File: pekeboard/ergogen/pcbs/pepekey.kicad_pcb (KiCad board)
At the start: 2 copper layers, 150.9 x 124.7 mm, 63 parts

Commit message: pekepad folder fix
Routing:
- net (no net): track 0.00 -> 337.7 mm
- net P008: track 268.6 -> 42.3 mm
- net P031: track 206.8 -> 0.00 mm, vias 6 -> 0
- net P100: track 258.8 -> 52.9 mm, vias 6 -> 5
- net P011: track 258.2 -> 52.9 mm, vias 6 -> 5
- net P106: track 251.5 -> 52.9 mm, vias 7 -> 5
- net P022: track 240.4 -> 42.3 mm, vias 5 -> 4
- net P024: track 230.4 -> 42.3 mm
- net P115: track 164.6 -> 0.00 mm, vias 6 -> 0
- net P002: track 158.9 -> 0.00 mm, vias 6 -> 0
- net P113: track 154.5 -> 0.00 mm, vias 3 -> 0
- net P025: track 120.0 -> 0.00 mm, vias 6 -> 0
- net GND: track 89.7 -> 0.00 mm, vias 2 -> 0
- net RAW: track 56.1 -> 0.00 mm, vias 1 -> 0
- net RST: track 47.5 -> 0.00 mm
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
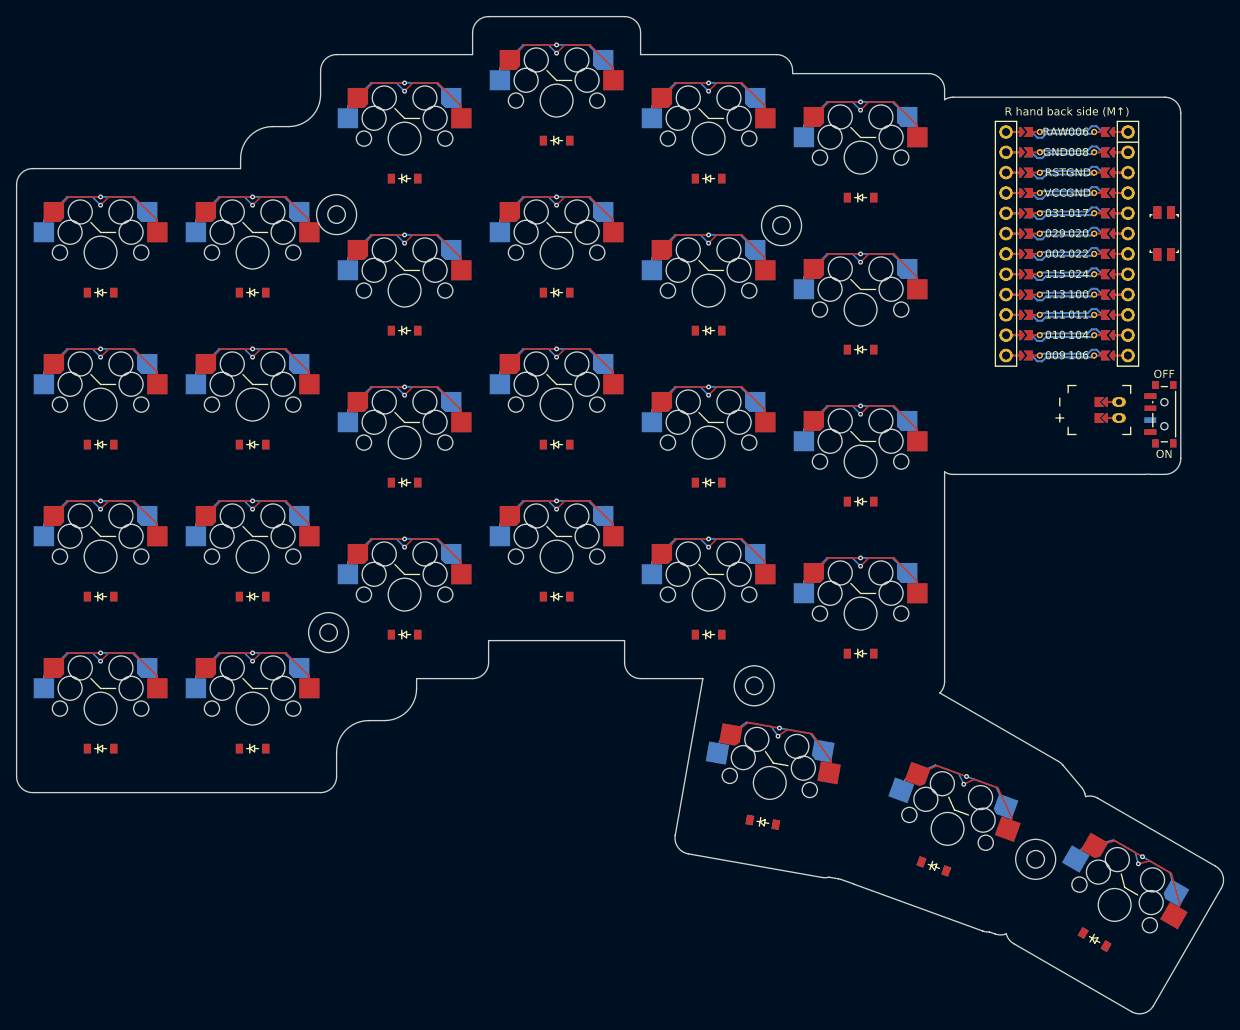
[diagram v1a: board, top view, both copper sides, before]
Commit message: Less spread for thumb cluster
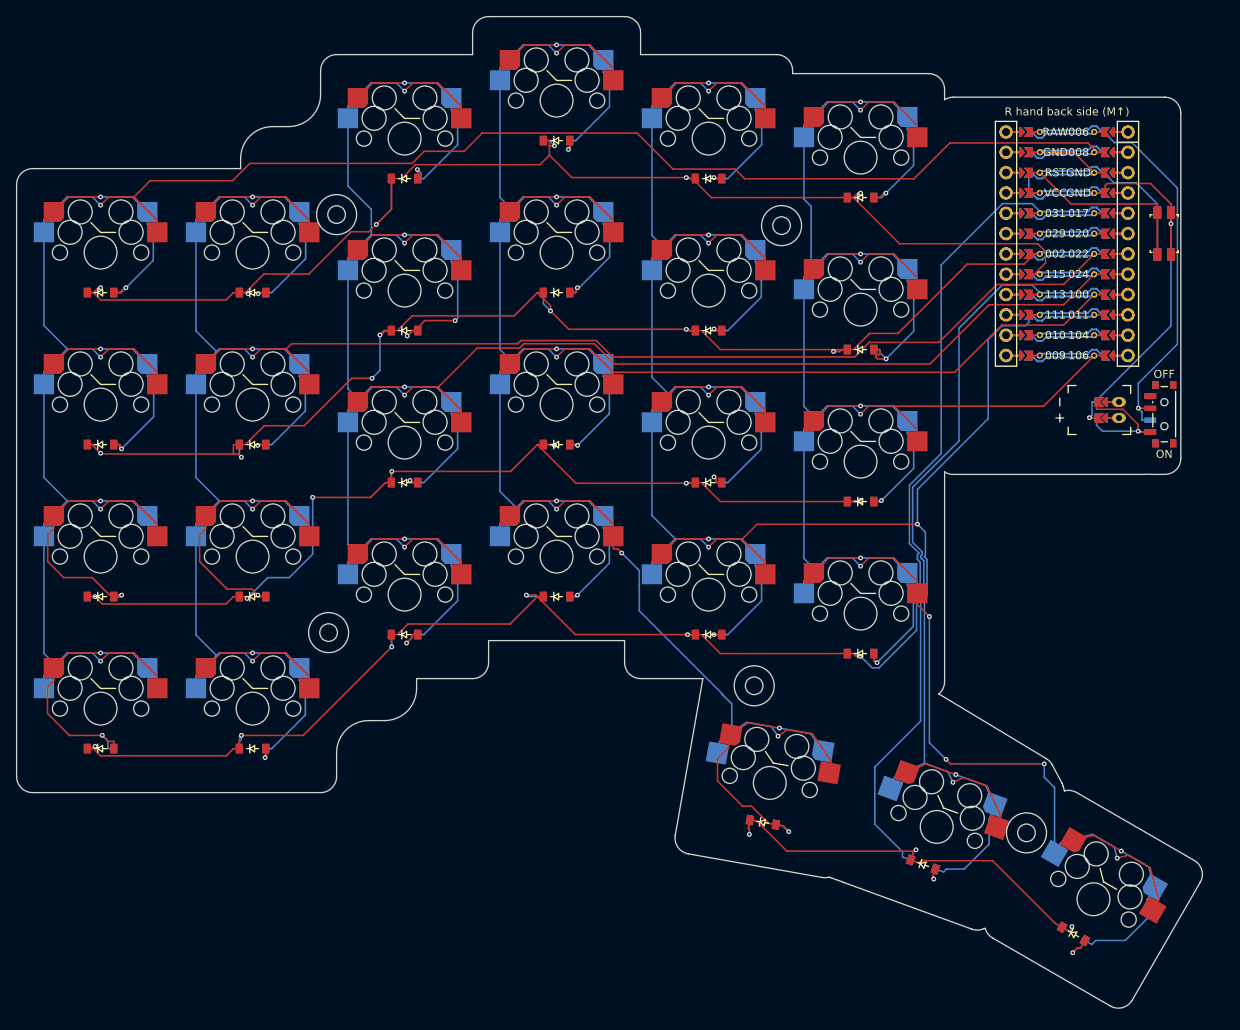
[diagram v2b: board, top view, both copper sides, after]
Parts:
- moved MH5 3.50 mm to (215.7, 135.5)
- moved S27 2.74 mm to (224.1, 143.8)
- moved D27 2.74 mm to (221.6, 148.2)
- moved D26 1.37 mm to (202.8, 139.5)
- moved S26 1.37 mm to (204.5, 134.8)
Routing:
- net (no net): track 337.7 -> 0.00 mm
- net P008: track 42.3 -> 268.6 mm
- net P031: track 0.00 -> 206.2 mm, vias 0 -> 6
- net P022: track 42.3 -> 247.5 mm
- net P100: track 52.9 -> 257.9 mm, vias 5 -> 6
- net P011: track 52.9 -> 248.8 mm, vias 5 -> 6
- net P024: track 42.3 -> 231.2 mm
- net P106: track 52.9 -> 237.5 mm, vias 5 -> 8
- net P115: track 0.00 -> 169.0 mm, vias 0 -> 6
- net P002: track 0.00 -> 163.3 mm, vias 0 -> 7
- net P113: track 0.00 -> 152.4 mm, vias 0 -> 3
- net P025: track 0.00 -> 123.5 mm, vias 0 -> 7
- net GND: track 0.00 -> 88.8 mm, vias 0 -> 2
- net RAW: track 0.00 -> 56.0 mm, vias 0 -> 1
- net RST: track 0.00 -> 47.5 mm
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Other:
- board size 150.9 x 124.7 mm -> 148.2 x 123.9 mm
- rule pad_to_mask_clearance: 0.05 -> 0
